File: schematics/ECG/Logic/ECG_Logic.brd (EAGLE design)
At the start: 27.3 x 27.3 mm, 72 parts, among them IC1 ADS1293, IC2 LIS3DH, IC3 MCP1703, IC4 CC2541, IC5 FSA4157, IC6 FSA4157, IC7 FSA4157, X1 XTAL-2SMD, X2 XTAL_403, X3 XTAL-CSM7

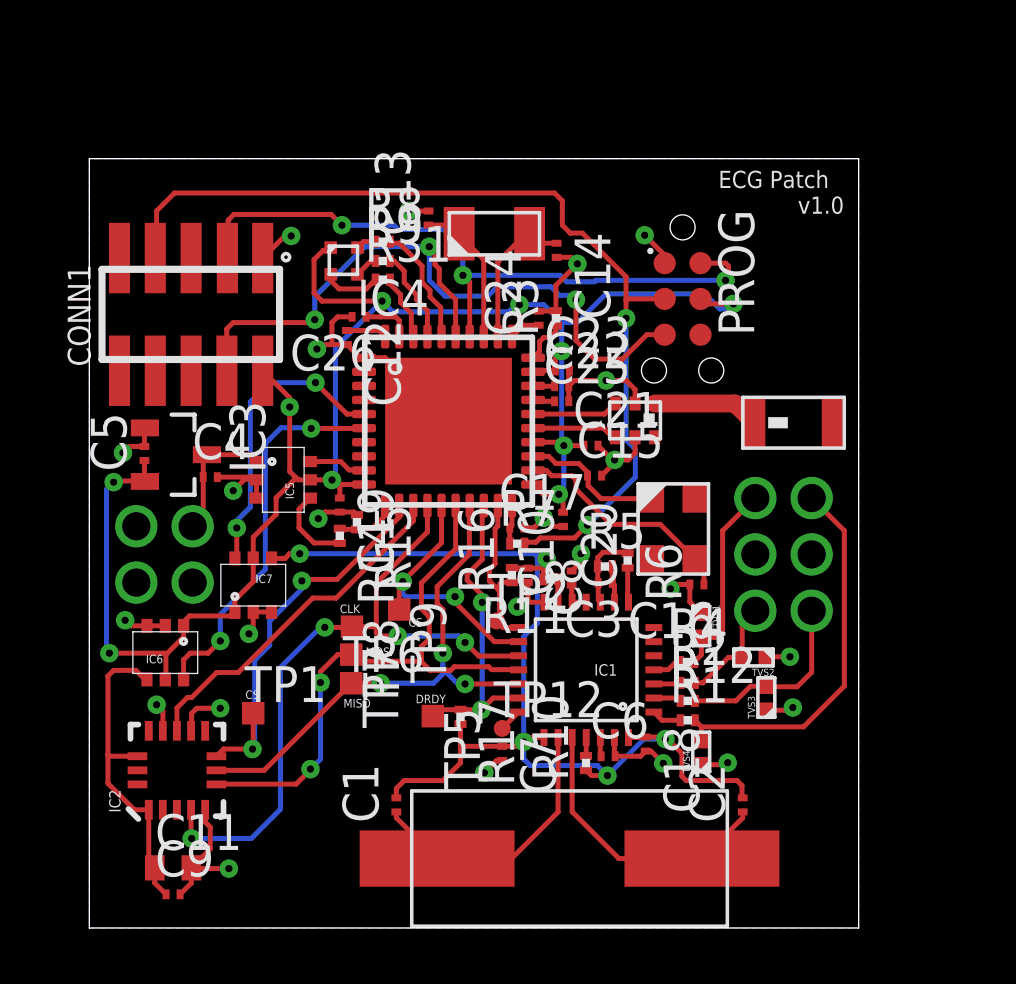
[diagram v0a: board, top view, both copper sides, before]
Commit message: moved batt scaled wire to ADC port 0 pin, updated routing. new gerbers generated for ordering v1.0 board
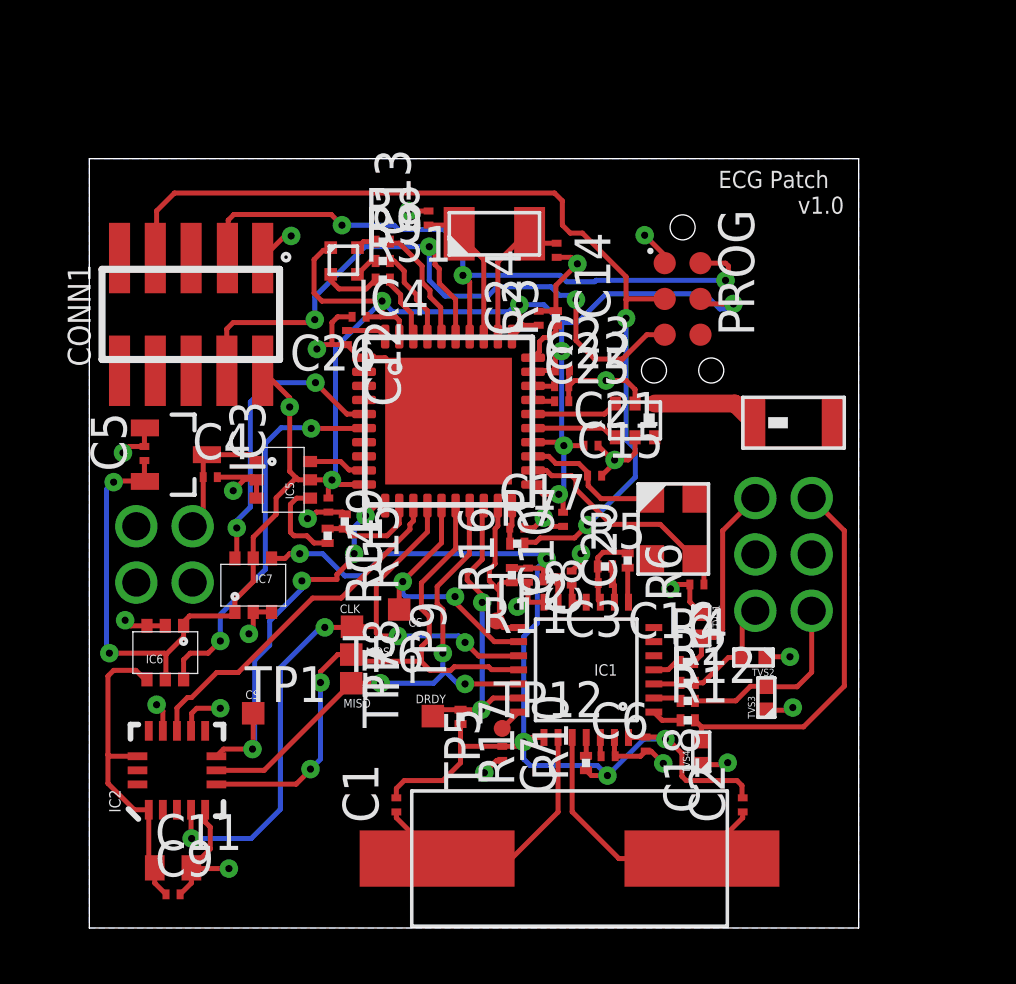
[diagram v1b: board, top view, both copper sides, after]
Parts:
- moved R15 0.43 mm to (9.07, 14.4)
- moved R14 0.43 mm to (8.46, 13.9)
- moved C19 0.41 mm to (8.48, 15.0)
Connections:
- net BATT_SCALED: now also IC4.12; no longer IC4.11
- net SPI_SS_ACCEL: now also IC4.11; no longer IC4.12
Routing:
- net BATT_SCALED: track 2.18 -> 3.50 mm
- net ECG_VCC: track 39.1 -> 39.7 mm
- net SPI_SS_ACCEL: vias 2 -> 4

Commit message: added comments to board
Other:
- board text added: "spring loaded header: switch pins 4 and 6 for VCC detection"
- board text added: "verify switch logic"
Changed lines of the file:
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@@
 <text x="5.5372" y="8.128" size="0.3048" layer="21">CS</text>
 <text x="11.3284" y="10.6934" size="0.3048" layer="21">CS</text>
+<text x="0.0762" y="27.9654" size="0.4064" layer="48">spring loaded header: switch pins 4 and 6 for VCC detection</text>
+<text x="0.0762" y="28.5242" size="0.4064" layer="21">verify switch logic</text>
 </plain>
 <attributes>

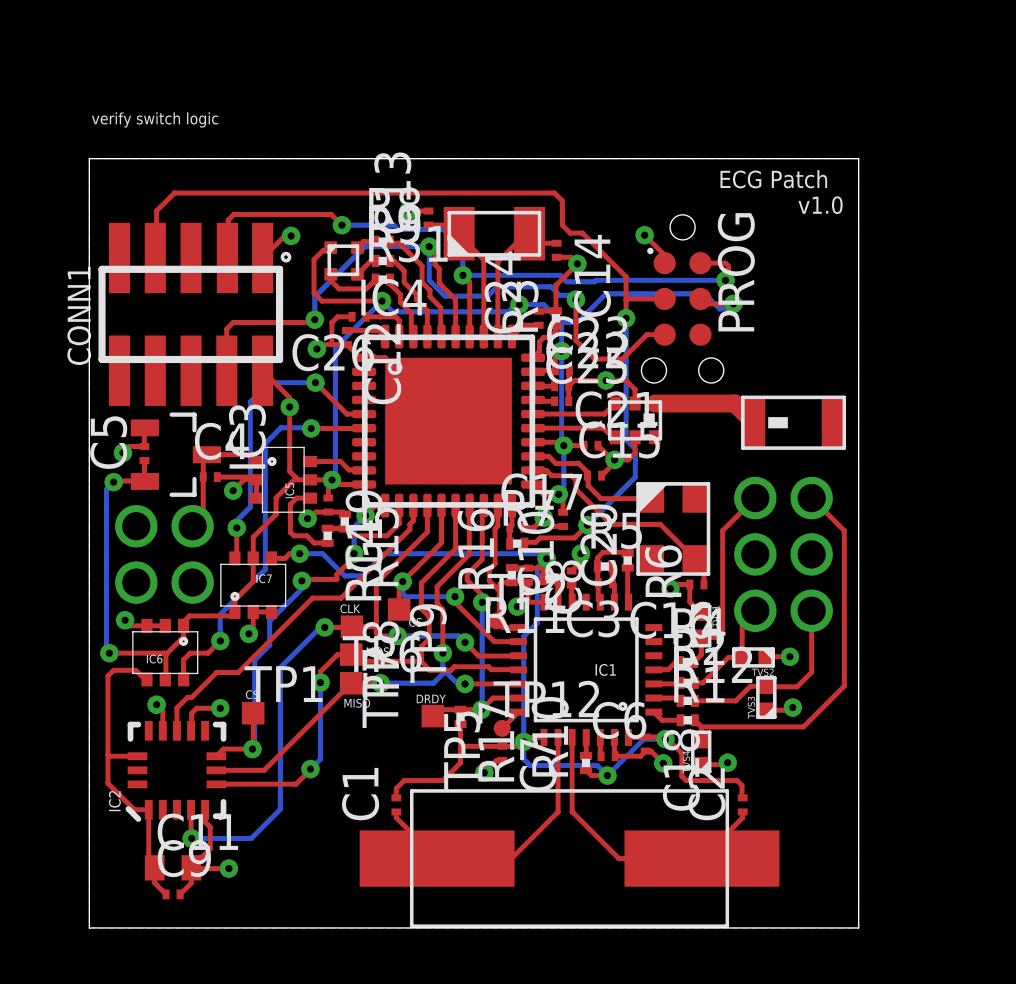
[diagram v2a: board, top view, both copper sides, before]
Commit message: replaced ADS1293 crystal with LTC6907. Fixed 6 pin programming header wiring
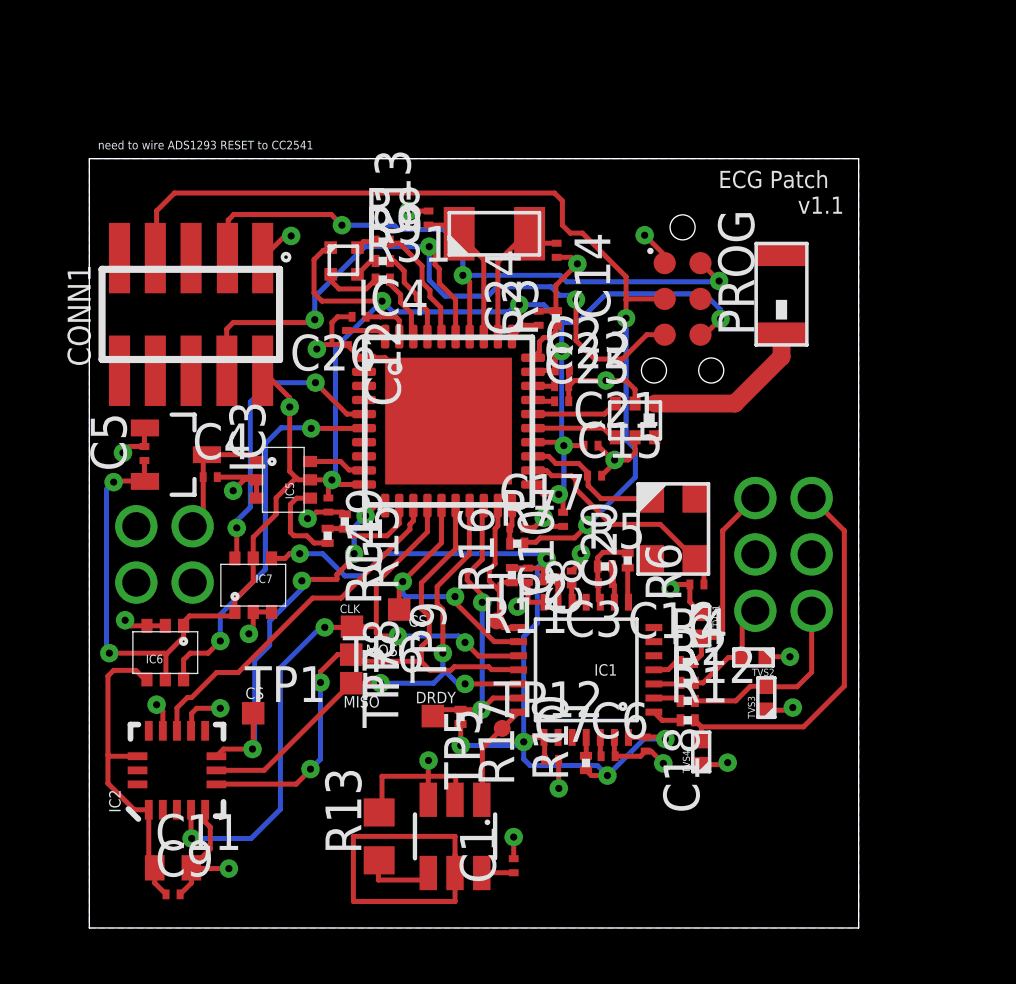
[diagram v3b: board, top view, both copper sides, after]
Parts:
- removed C2: 22pF, rcl:C0201
- removed X3: XTAL-CSM7, ecs:CSM-7
- added IC9: LTC6907, linear:TSOT23-6
- added R13: 50K, rcl:R0603
- C1: value 22pF -> 0.1uF
- moved C1 4.69 mm to (15.1, 2.21)
- moved RF 4.66 mm to (24.6, 22.6), turned to 270 degrees
- moved C7 1.77 mm to (16.4, 5.97), turned to 0 degrees
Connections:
- removed net XTAL1: C1.1, IC1.23, X3.1
- removed net XTAL2: C2.1, IC1.24, X3.2
- new net GRD: IC9.5
- new net N$14: IC9.4, R13.1
- new net V+: C1.1, IC9.6
- net CLK: now also IC9.1
- net ECG_VCC: no longer C1.2, C2.2
- net GND: now also C1.2, IC9.2, IC9.3, R13.2
- net VCC: now also PROG.6; no longer PROG.4
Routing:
- net GRD: track 0.00 -> 11.8 mm
- net XTAL2: track 10.2 -> 0.00 mm
- net XTAL1: track 9.88 -> 0.00 mm
- net GND: track 51.1 -> 58.3 mm, vias 24 -> 26
- net ECG_VCC: track 39.7 -> 32.5 mm, vias 5 -> 6
- net CLK: track 0.82 -> 3.65 mm
- net N$14: track 0.00 -> 2.74 mm
- net N$6: track 3.81 -> 6.01 mm
- net V+: track 0.00 -> 1.14 mm
- net P2_2/DC: track 24.5 -> 23.6 mm
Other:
- board text added: "Added LTC6907 , C1, and R13 (PNM0603E5002BST5)"
- board text added: "need to wire ADS1293 RESET to CC2541"
- board text added: "removed X3,C1,C2"
- board text added: "there is a 200uS startup delay @4MHz so wire LTC6907 VCC pin to CC2541"
- board text added: "v1.1"
- board text removed: "spring loaded header: switch pins 4 and 6 for VCC detection"
- board text removed: "v1.0"
- board text removed: "verify switch logic"

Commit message: replaced vertical headers with right angle spring loaded headers. routed osc power to pin2 of cc2541
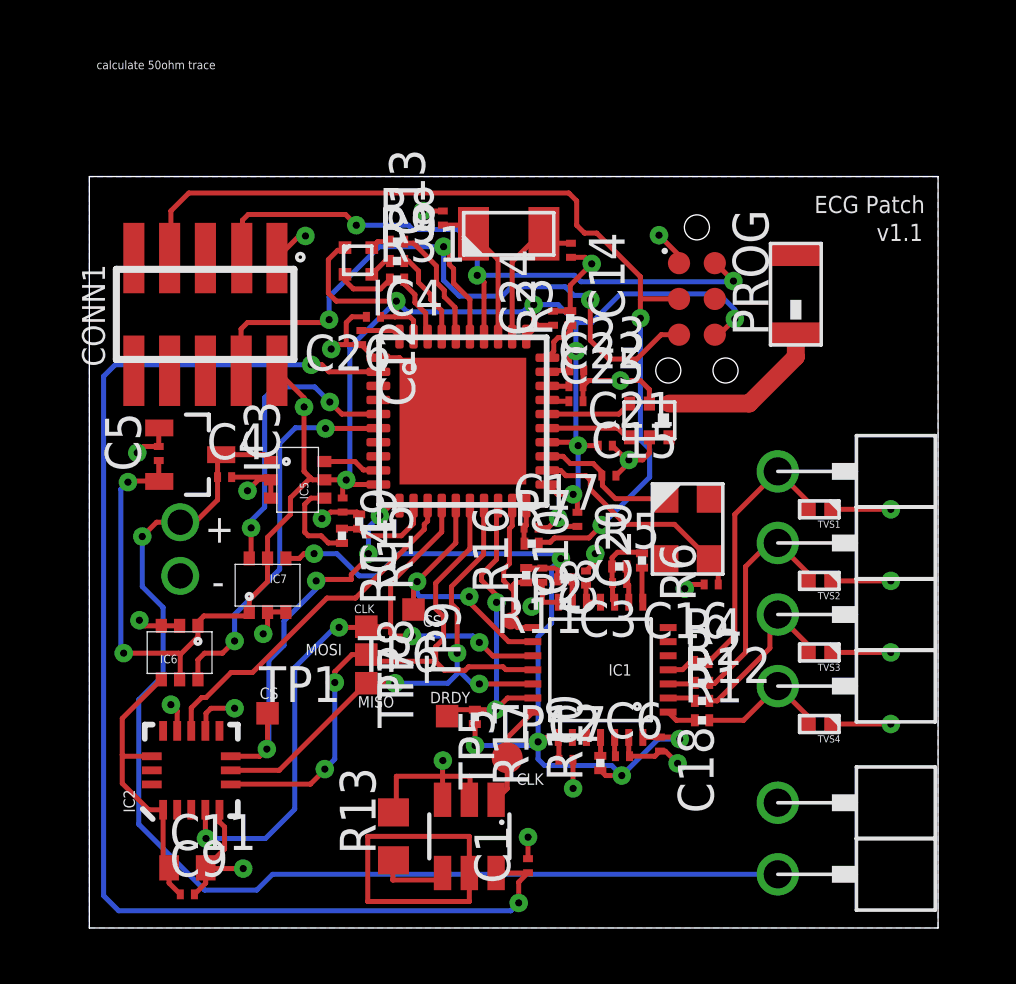
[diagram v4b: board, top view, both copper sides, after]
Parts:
- removed CONN2: M80-4V, harwin:M80-4-V
- removed CONN3: M80-6V, harwin:M80-6-V
- added U$1, U$2, U$3, U$4, U$5, U$6: TARGET_RA, pins:TARGET_RA
- TP12: value TPSTP06R -> TPSTP11R; device testpad:TP06R -> testpad:TP11R
- moved TVS1 5.89 mm to (25.9, 14.9), turned to 180 degrees
- moved TVS4 4.31 mm to (25.9, 7.24), turned to 180 degrees
- moved TVS2 3.58 mm to (25.9, 12.3)
- moved TVS3 2.47 mm to (25.9, 9.78), turned to 180 degrees
- moved TP12 1.06 mm to (14.8, 6.04)
- moved TP6 0.53 mm to (9.83, 8.69)
- moved TP7 0.53 mm to (9.83, 9.70)
- moved C10 0.51 mm to (17.6, 12.4)
- moved C16 0.51 mm to (22.1, 12.2)
- moved C21 0.51 mm to (18.3, 17.1)
- moved IC1 0.51 mm to (18.1, 9.16)
- moved IC8 0.51 mm to (19.8, 18.0)
- moved RF 0.51 mm to (25.1, 22.6)
- moved C17 0.51 mm to (15.7, 14.2)
- moved C19 0.51 mm to (8.99, 15.0)
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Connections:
- removed net V+: C1.1, IC9.6
- new net ADS1923_OSC_VCC: C1.1, IC4.2, IC9.6
- net BATT: now also U$6.1; no longer CONN2.1
- net GND: now also U$5.1; no longer CONN2.2
- net LA: now also U$2.1; no longer CONN3.1
- net LL: now also U$1.1; no longer CONN3.6
- net RA: now also U$3.1; no longer CONN3.3
- net RL: now also U$4.1; no longer CONN3.4
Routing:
- net ADS1923_OSC_VCC: track 0.00 -> 45.9 mm, vias 0 -> 2
- net BATT: track 4.75 -> 41.5 mm, vias 0 -> 2
- net RA: track 13.6 -> 4.73 mm
- net GND: track 58.3 -> 62.7 mm, vias 26 -> 28
- net LL: track 3.90 -> 8.08 mm
- net RL: track 7.01 -> 9.57 mm
- net V+: track 1.14 -> 0.00 mm
- net ACCEL_VCC: track 11.6 -> 10.5 mm
- net LA: track 6.76 -> 6.03 mm
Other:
- board size 27.3 x 27.3 mm -> 30.1 x 26.7 mm
- board text added: "+"
- board text added: "-"
- board text added: "calculate 50ohm trace"
- board text added: "review/fix LEDs?"
- board text removed: "need to wire ADS1293 RESET to CC2541"
- board text removed: "there is a 200uS startup delay @4MHz so wire LTC6907 VCC pin to CC2541"

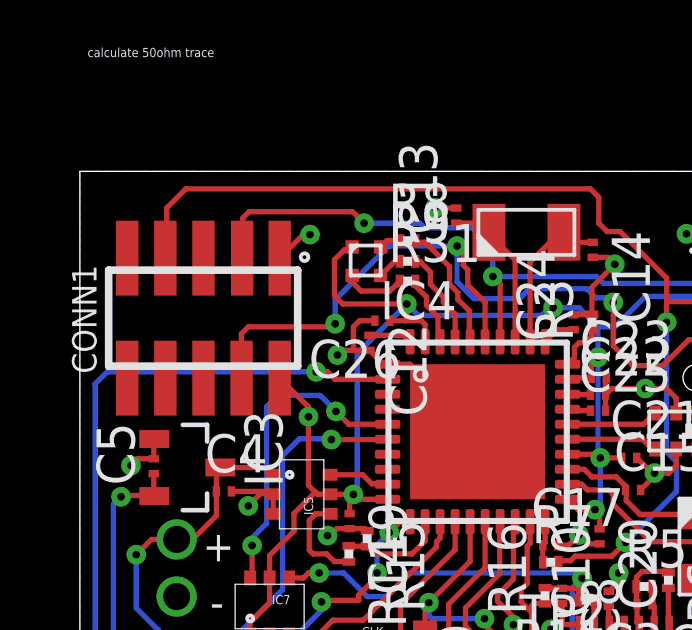
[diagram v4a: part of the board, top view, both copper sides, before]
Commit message: switched ECG boards to spring loaded pin headers
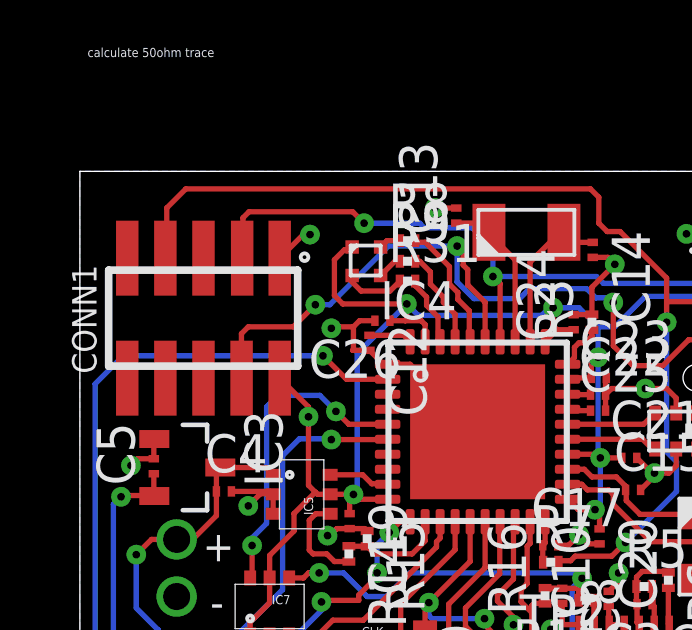
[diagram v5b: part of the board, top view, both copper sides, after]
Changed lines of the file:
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@@
 <setting verticaltext="up"/>
 </settings>
-<grid distance="1" unitdist="mil" unit="mil" style="lines" multiple="1" display="yes" altdistance="0.025" altunitdist="inch" altunit="inch"/>
+<grid distance="1" unitdist="mil" unit="inch" style="lines" multiple="1" display="yes" altdistance="0.025" altunitdist="inch" altunit="inch"/>
 <layers>
 <layer number="1" name="Top" color="4" fill="1" visible="yes" active="yes"/>
@@
 <via x="17.8308" y="23.5712" extent="1-16" drill="0.254"/>
 <wire x1="10.2402" y1="20.2224" x2="10.2578" y2="20.24" width="0.1778" layer="1"/>
-<via x="8.5852" y="20.5486" extent="1-16" drill="0.254"/>
+<via x="8.382" y="21.4376" extent="1-16" drill="0.254"/>
 <wire x1="12.5476" y1="25.4468" x2="11.8404" y2="25.4468" width="0.1778" layer="1"/>
 <wire x1="10.2578" y1="20.24" x2="10.117" y2="20.24" width="0.1778" layer="1"/>
@@
 <wire x1="11.0078" y1="20.24" x2="13.2578" y2="17.99" width="0.1778" layer="1"/>
 <wire x1="9.652" y1="20.705" x2="9.0932" y2="20.705" width="0.1778" layer="1"/>
-<wire x1="9.0932" y1="20.705" x2="8.7416" y2="20.705" width="0.1778" layer="1"/>
 <wire x1="9.8338" y1="21.6916" x2="9.3218" y2="21.6916" width="0.1778" layer="1"/>
 <wire x1="9.3218" y1="21.6916" x2="9.1186" y2="21.4884" width="0.1778" layer="1"/>
@@
 <contactref element="PROG" pad="1"/>
 <wire x1="9.1186" y1="20.7304" x2="9.0932" y2="20.705" width="0.1778" layer="1"/>
-<wire x1="8.7416" y1="20.705" x2="8.5852" y2="20.5486" width="0.1778" layer="1"/>
 <via x="1.7018" y="16.8656" extent="1-16" drill="0.254"/>
 <via x="5.6134" y="15.5194" extent="1-16" drill="0.254"/>
@@
 <wire x1="26.3588" y1="7.239" x2="28.448" y2="7.239" width="0.1778" layer="1"/>
 <via x="3.2258" y="12.4968" extent="1-16" drill="0.9"/>
+<wire x1="9.1186" y1="21.4884" x2="8.4328" y2="21.4884" width="0.1778" layer="1"/>
+<wire x1="8.4328" y1="21.4884" x2="8.382" y2="21.4376" width="0.1778" layer="1"/>
 </signal>
 <signal name="IN1">
@@
 <via x="12.573" y="24.1808" extent="1-16" drill="0.254"/>
 <wire x1="13.5128" y1="20.995" x2="13.5078" y2="20.99" width="0.1778" layer="1"/>
-<wire x1="5.6134" y1="21.4884" x2="8.4074" y2="21.4884" width="0.1778" layer="1"/>
-<wire x1="8.4074" y1="21.4884" x2="8.509" y2="21.59" width="0.1778" layer="1"/>
-<via x="8.509" y="21.59" extent="1-16" drill="0.254"/>
-<wire x1="8.509" y1="21.59" x2="8.509" y2="22.4028" width="0.1778" layer="16"/>
-<wire x1="8.509" y1="22.4028" x2="10.287" y2="24.1808" width="0.1778" layer="16"/>
+<via x="7.8486" y="22.225" extent="1-16" drill="0.254"/>
+<wire x1="8.3312" y1="22.225" x2="10.287" y2="24.1808" width="0.1778" layer="16"/>
 <wire x1="13.5078" y1="20.99" x2="13.5078" y2="22.3062" width="0.1778" layer="1"/>
 <wire x1="13.5078" y1="22.3062" x2="12.9286" y2="22.8854" width="0.1778" layer="1"/>
@@
 <wire x1="17.78" y1="22.3012" x2="17.78" y2="20.8534" width="0.1778" layer="1"/>
 <wire x1="17.78" y1="20.8534" x2="18.4404" y2="20.193" width="0.1778" layer="1"/>
+<wire x1="5.6134" y1="21.4884" x2="7.112" y2="21.4884" width="0.1778" layer="1"/>
+<wire x1="7.112" y1="21.4884" x2="7.8486" y2="22.225" width="0.1778" layer="1"/>
+<wire x1="7.8486" y1="22.225" x2="8.3312" y2="22.225" width="0.1778" layer="16"/>
 </signal>
 <signal name="P2_3/32K_Q2">
@@
 <wire x1="14.4374" y1="1.9512" x2="15.5616" y2="1.9512" width="0.1778" layer="1"/>
 <wire x1="15.5616" y1="1.9512" x2="15.5702" y2="1.9598" width="0.1778" layer="1"/>
-<wire x1="10.2578" y1="19.74" x2="8.5048" y2="19.74" width="0.1778" layer="1"/>
-<wire x1="8.5048" y1="19.74" x2="8.255" y2="19.9898" width="0.1778" layer="1"/>
-<wire x1="8.255" y1="19.9898" x2="7.874" y2="19.9898" width="0.1778" layer="1"/>
-<via x="7.874" y="19.9898" extent="1-16" drill="0.254"/>
-<wire x1="7.874" y1="19.9898" x2="0.9144" y2="19.9898" width="0.1778" layer="16"/>
-<wire x1="0.9144" y1="19.9898" x2="0.508" y2="19.5834" width="0.1778" layer="16"/>
+<via x="8.1026" y="20.5232" extent="1-16" drill="0.254"/>
 <wire x1="0.508" y1="19.5834" x2="0.508" y2="1.143" width="0.1778" layer="16"/>
 <wire x1="0.508" y1="1.143" x2="1.0414" y2="0.6096" width="0.1778" layer="16"/>
@@
 <wire x1="1.0414" y1="0.6096" x2="14.9606" y2="0.6096" width="0.1778" layer="16"/>
 <wire x1="14.9606" y1="0.6096" x2="15.24" y2="0.889" width="0.1778" layer="16"/>
+<wire x1="8.1026" y1="20.5232" x2="1.4478" y2="20.5232" width="0.1778" layer="16"/>
+<wire x1="1.4478" y1="20.5232" x2="0.508" y2="19.5834" width="0.1778" layer="16"/>
+<wire x1="10.2578" y1="19.74" x2="8.8858" y2="19.74" width="0.1778" layer="1"/>
+<wire x1="8.8858" y1="19.74" x2="8.1026" y2="20.5232" width="0.1778" layer="1"/>
 </signal>
 </signals>
